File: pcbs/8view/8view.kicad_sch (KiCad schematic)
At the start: 40 parts, among them J1 Conn_01x10_Female, J2 Conn_01x10_Female, J3 Conn_01x06_Female, J4 Conn_01x06_Female, U1 ATtiny828-A, U2 HDSP-A151, U3 HDSP-A151

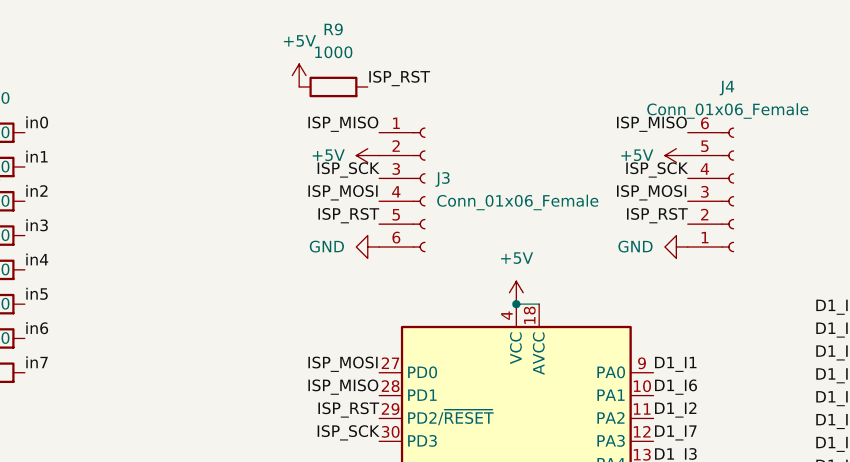
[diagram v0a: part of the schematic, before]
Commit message: v1 8view borads
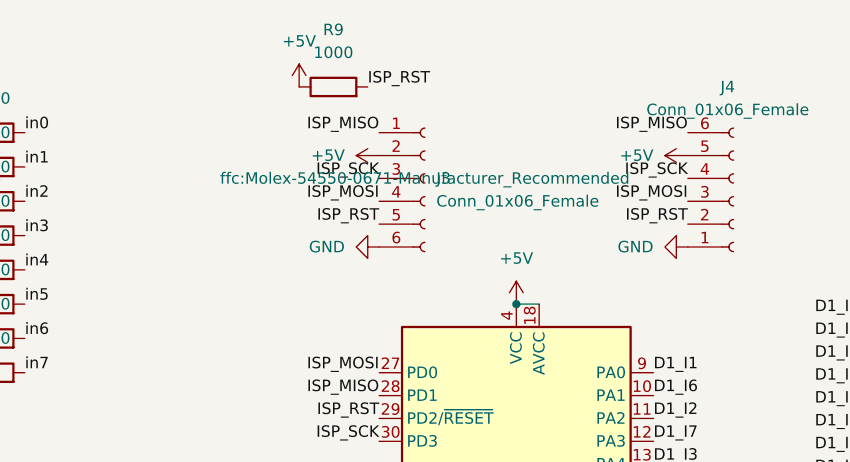
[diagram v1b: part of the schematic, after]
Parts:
- J1, J2: footprint Connector_PinSocket_2.54mm:PinSocket_1x08_P2.54mm_Horizontal -> Connector_PinHeader_2.54mm:PinHeader_1x08_P2.54mm_Horizontal
- J3, J4: footprint Connector_FFC-FPC:TE_0-1734839-6_1x06-1MP_P0.5mm_Horizontal -> ffc:Molex-54550-0671-Manufacturer_Recommended
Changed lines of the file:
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@@
       (effects (font (size 1.27 1.27)) (justify left))
     )
-    (property "Footprint" "Connector_PinSocket_2.54mm:PinSocket_1x08_P2.54mm_Horizontal" (id 2) (at 133.35 88.9 0)
+    (property "Footprint" "Connector_PinHeader_2.54mm:PinHeader_1x08_P2.54mm_Horizontal" (id 2) (at 133.35 88.9 0)
       (effects (font (size 1.27 1.27)) hide)
     )
@@
     (property "Reference" "J4" (id 0) (at 220.345 31.75 0))
     (property "Value" "Conn_01x06_Female" (id 1) (at 220.345 34.29 0))
-    (property "Footprint" "Connector_FFC-FPC:TE_0-1734839-6_1x06-1MP_P0.5mm_Horizontal" (id 2) (at 220.98 44.45 0)
+    (property "Footprint" "ffc:Molex-54550-0671-Manufacturer_Recommended" (id 2) (at 220.98 44.45 0)
       (effects (font (size 1.27 1.27)) hide)
     )
@@
     (property "Reference" "J2" (id 0) (at 132.715 101.6 0))
     (property "Value" "Conn_01x10_Female" (id 1) (at 132.715 104.14 0))
-    (property "Footprint" "Connector_PinSocket_2.54mm:PinSocket_1x08_P2.54mm_Horizontal" (id 2) (at 133.35 119.38 0)
+    (property "Footprint" "Connector_PinHeader_2.54mm:PinHeader_1x08_P2.54mm_Horizontal" (id 2) (at 133.35 119.38 0)
       (effects (font (size 1.27 1.27)) hide)
     )
@@
       (effects (font (size 1.27 1.27)) (justify left))
     )
-    (property "Footprint" "Connector_FFC-FPC:TE_0-1734839-6_1x06-1MP_P0.5mm_Horizontal" (id 2) (at 186.69 41.91 0)
-      (effects (font (size 1.27 1.27)) hide)
-    )
+    (property "Footprint" "ffc:Molex-54550-0671-Manufacturer_Recommended" (id 2) (at 186.69 41.91 0))
     (property "Datasheet" "~" (id 3) (at 186.69 41.91 0)
       (effects (font (size 1.27 1.27)) hide)
@@
     )
     (path "/13c33d59-1d6b-4a21-bf64-0f05018cc6c0"
-      (reference "J1") (unit 1) (value "Conn_01x10_Female") (footprint "Connector_PinSocket_2.54mm:PinSocket_1x08_P2.54mm_Horizontal")
+      (reference "J1") (unit 1) (value "Conn_01x10_Female") (footprint "Connector_PinHeader_2.54mm:PinHeader_1x08_P2.54mm_Horizontal")
     )
     (path "/44a29a93-aaef-47c1-b31e-ff16a5a6c45b"
-      (reference "J2") (unit 1) (value "Conn_01x10_Female") (footprint "Connector_PinSocket_2.54mm:PinSocket_1x08_P2.54mm_Horizontal")
+      (reference "J2") (unit 1) (value "Conn_01x10_Female") (footprint "Connector_PinHeader_2.54mm:PinHeader_1x08_P2.54mm_Horizontal")
     )
     (path "/45351f59-8250-4d09-8ac8-09f9b1bb3e1a"
-      (reference "J3") (unit 1) (value "Conn_01x06_Female") (footprint "Connector_FFC-FPC:TE_0-1734839-6_1x06-1MP_P0.5mm_Horizontal")
+      (reference "J3") (unit 1) (value "Conn_01x06_Female") (footprint "ffc:Molex-54550-0671-Manufacturer_Recommended")
     )
     (path "/28a246ad-e60f-4785-89f7-346ae3ea6fea"
-      (reference "J4") (unit 1) (value "Conn_01x06_Female") (footprint "Connector_FFC-FPC:TE_0-1734839-6_1x06-1MP_P0.5mm_Horizontal")
+      (reference "J4") (unit 1) (value "Conn_01x06_Female") (footprint "ffc:Molex-54550-0671-Manufacturer_Recommended")
     )
     (path "/9dfd4deb-2dbb-459c-b795-c62a796da71f"

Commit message: 8view: 10pin skirt, 1.5k leds
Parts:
- removed J2: Conn_01x10_Female, Connector_PinHeader_2.54mm:PinHeader_1x08_P2.54mm_Horizontal, symbol Connector:Conn_01x08_Female
- added J2: Conn_01x10_Female, Connector_PinHeader_2.54mm:PinHeader_1x10_P2.54mm_Horizontal, symbol Connector:Conn_01x10_Female
- added R10: 1k5, Resistor_SMD:R_0402_1005Metric, symbol Device:R
- R1, R2, R3, R4, R5, R6, R7, R8, R9: value 1000 -> 1k5
- R11: renamed from R10; value 1000 -> 1k
- R12: renamed from R11; value 1000 -> 1k
- R13: renamed from R12; value 1000 -> 1k
- R14: renamed from R13; value 1000 -> 1k
- R15: renamed from R14; value 1000 -> 1k
- R16: renamed from R15; value 1000 -> 1k
- R17: renamed from R16; value 1000 -> 1k
- R18: renamed from R17; value 1000 -> 1k
- R19: renamed from R18; value 1000 -> 1k
- R20: renamed from R19; value 1000 -> 1k
- R21: renamed from R20; value 1000 -> 1k
- R22: renamed from R21; value 1000 -> 1k
- R23: renamed from R22; value 1000 -> 1k
- R24: renamed from R23; value 1000 -> 1k
- R25: renamed from R24; value 1000 -> 1k
- R26: renamed from R25; value 1000 -> 1k
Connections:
- net +5V: now also J2.10 (Pin_10)
- net GND: now also J2.1 (Pin_1)
- net ISP_RST: now also R10.2; no longer R9.2
- net in0: now also J2.9 (Pin_9)
- net in1: now also J2.8 (Pin_8)
- net in2: now also J2.7 (Pin_7)
- net in3: now also J2.6 (Pin_6)
- net in4: now also J2.5 (Pin_5)
- net in5: now also J2.4 (Pin_4)
- net in6: now also J2.3 (Pin_3)
- net in7: now also J2.2 (Pin_2)
- new net: R10.1, R9.2
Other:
- moved on the sheet: D1, R1, R9
